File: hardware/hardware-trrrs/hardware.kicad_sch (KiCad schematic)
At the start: 81 parts, among them J2 Barrel_Jack, M1 Stepper_Motor_unipolar_5pin, M10 Stepper_Motor_unipolar_5pin, M11 Stepper_Motor_unipolar_5pin, M12 Stepper_Motor_unipolar_5pin, M13 Stepper_Motor_unipolar_5pin, M14 Stepper_Motor_unipolar_5pin, M2 Stepper_Motor_unipolar_5pin, M3 Stepper_Motor_unipolar_5pin, M4 Stepper_Motor_unipolar_5pin, M5 Stepper_Motor_unipolar_5pin, M6 Stepper_Motor_unipolar_5pin, M7 Stepper_Motor_unipolar_5pin, M8 Stepper_Motor_unipolar_5pin, M9 Stepper_Motor_unipolar_5pin, SW1 SW_Push_SPDT, SW10 SW_Push_SPDT, SW11 SW_Push_SPDT, SW12 SW_Push_SPDT, SW13 SW_Push_SPDT, SW14 SW_Push_SPDT, SW15 SW_Push_SPDT, SW16 SW_Push_SPDT, SW2 SW_Push_SPDT, SW3 SW_Push_SPDT, SW4 SW_Push_SPDT, SW5 SW_Push_SPDT, SW6 SW_Push_SPDT, SW7 SW_Push_SPDT, SW8 SW_Push_SPDT, SW9 SW_Push_SPDT, U1 WeMos_D1_mini, U10 ULN2003A, U11 ULN2003A, U12 ULN2003A, U13 ULN2003A, U14 ULN2003A, U15 ULN2003A, U16 ULN2003A, U17 ULN2003A, U2 CD4051B, U3 CD4051B, U4 ULN2003A, U5 ULN2003A, U6 ULN2003A, U7 ULN2003A, U8 ULN2003A, U9 ULN2003A

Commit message: added new pcb revision (trrrs)
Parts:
- added C15, C16: 10pF, Capacitor_SMD:C_0402_1005Metric, symbol Device:C
- added M15, M16: Stepper_Motor_unipolar_5pin, Connector_Audio:AUDIO-SMD_STX-3542-5N-G-TR, symbol Motor:Stepper_Motor_unipolar_5pin
- added U18, U19: ULN2003A, Package_SO:SOIC-16_3.9x9.9mm_P1.27mm, symbol Transistor_Array:ULN2003A
- C1, C10, C11, C12, C13, C14, C2, C3, C4, C5, C6, C7, C8, C9: footprint Capacitor_SMD:C_0805_2012Metric -> Capacitor_SMD:C_0402_1005Metric; LCSC PN C157608 -> C1545
- M1, M10, M11, M12, M13, M14, M2, M3, M4, M7, M8, M9: footprint Connector_Audio:HOOYA-PJ-3505A_C19190915-Jack_3.5mm_PJ31060-I_Horizontal -> Connector_Audio:AUDIO-SMD_STX-3542-5N-G-TR; LCSC PN C19190915 -> (none); LSCS PN (none) -> C157991
- M5, M6: footprint Connector_Audio:HOOYA-PJ-3505A_C19190915-Jack_3.5mm_PJ31060-I_Horizontal -> Connector_Audio:AUDIO-SMD_STX-3542-5N-G-TR; LSCS PN C19190915 -> C157991
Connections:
- net +5V: now also C15.1, C16.1, M15.1, M16.1, U18.9 (COM), U19.9 (COM)
- net GND: now also C15.2, C16.2, U18.8 (GND), U19.8 (GND)
- net IN1: now also U18.1 (I1), U19.1 (I1)
- net IN2: now also U18.2 (I2), U19.2 (I2)
- net IN3: now also U18.3 (I3), U19.3 (I3)
- net IN4: now also U18.4 (I4), U19.4 (I4)
- net PINK1: now also M1.4; no longer M1.3 (-)
- net PINK10: now also M10.4; no longer M10.3 (-)
- net PINK11: now also M11.4; no longer M11.3 (-)
- net PINK12: now also M12.4; no longer M12.3 (-)
- net PINK13: now also M13.4; no longer M13.3 (-)
- net PINK14: now also M14.4; no longer M14.3 (-)
- net PINK2: now also M2.4; no longer M2.3 (-)
- net PINK3: now also M3.4; no longer M3.3 (-)
- net PINK4: now also M4.4; no longer M4.3 (-)
- net PINK5: now also M5.4; no longer M5.3 (-)
- net PINK6: now also M6.4; no longer M6.3 (-)
- net PINK7: now also M7.4; no longer M7.3 (-)
- net PINK8: now also M8.4; no longer M8.3 (-)
- net PINK9: now also M9.4; no longer M9.3 (-)
- net YELLOW1: now also M1.3 (-); no longer M1.4
- net YELLOW10: now also M10.3 (-); no longer M10.4
- net YELLOW11: now also M11.3 (-); no longer M11.4
- net YELLOW12: now also M12.3 (-); no longer M12.4
- net YELLOW13: now also M13.3 (-); no longer M13.4
- net YELLOW14: now also M14.3 (-); no longer M14.4
- net YELLOW2: now also M2.3 (-); no longer M2.4
- net YELLOW3: now also M3.3 (-); no longer M3.4
- net YELLOW4: now also M4.3 (-); no longer M4.4
- net YELLOW5: now also M5.3 (-); no longer M5.4
- net YELLOW6: now also M6.3 (-); no longer M6.4
- net YELLOW7: now also M7.3 (-); no longer M7.4
- net YELLOW8: now also M8.3 (-); no longer M8.4
- net YELLOW9: now also M9.3 (-); no longer M9.4
- new net BLUE15: M15.5, U18.16 (O1)
- new net BLUE16: M16.5, U19.16 (O1)
- new net ORANGE15: M15.2, U18.13 (O4)
- new net ORANGE16: M16.2, U19.13 (O4)
- new net PINK15: M15.4, U18.15 (O2)
- new net PINK16: M16.4, U19.15 (O2)
- new net YELLOW15: M15.3 (-), U18.14 (O3)
- new net YELLOW16: M16.3 (-), U19.14 (O3)
- no-connect marks 89 -> 101
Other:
- note added: "CHOOSE YOUR COMPONENTS FROM HERE: https://jlcpcb.com/parts/2nd/Capacitors/Multilayer_Ceramic_Capacitors_MLCC_SMD_SMT_33?spm=search&searchTxt=10pf%20 the jlcpcb parts lib and not lcsc!!"
- note added: "good"
- moved on the sheet: C10, C11, C12, C13, C14, C5, C6, C7, C8, C9, U10, U11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

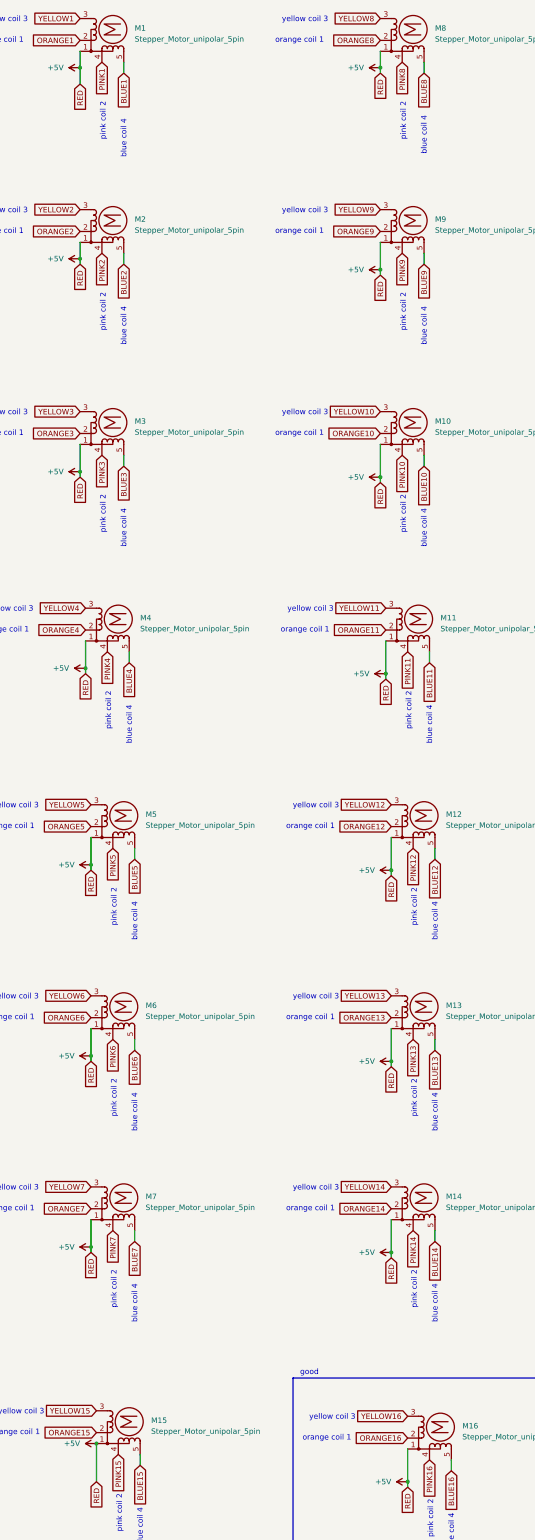
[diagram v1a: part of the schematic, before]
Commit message: Added do not populate flag to trrrs jacks
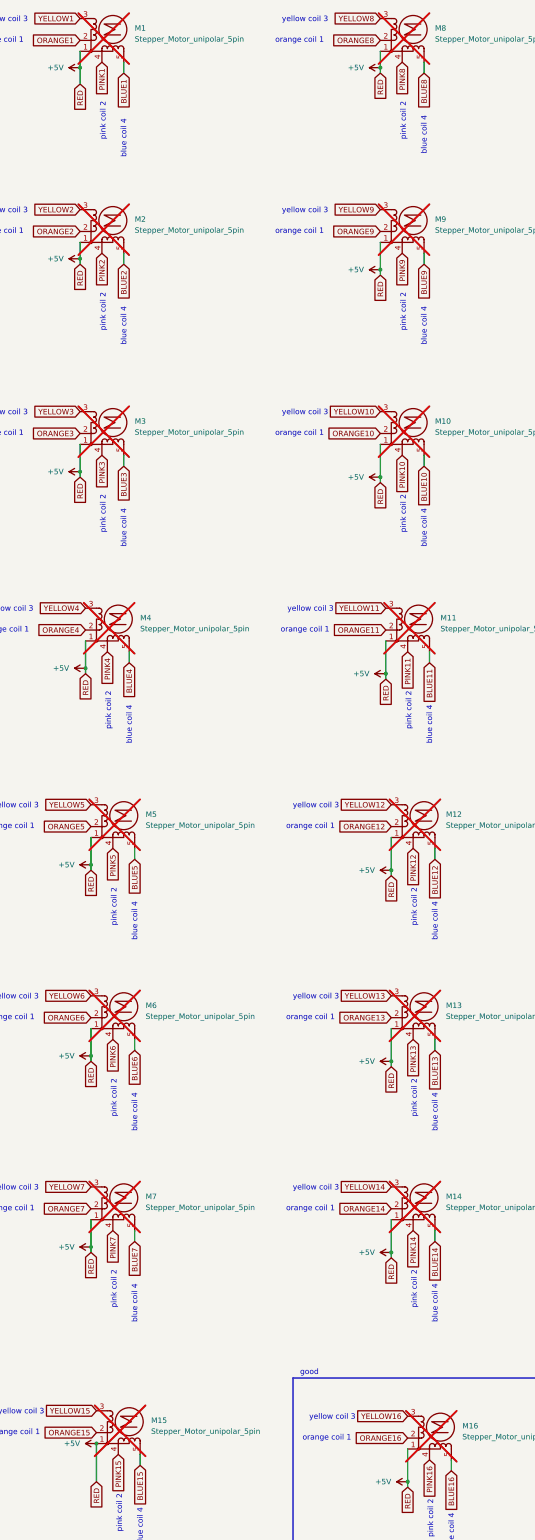
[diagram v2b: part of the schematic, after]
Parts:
- M1, M10, M11, M12, M13, M14, M15, M16, M2, M3, M4, M5, M6, M7, M8, M9: now not fitted
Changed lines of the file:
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@@
 		(in_bom yes)
 		(on_board yes)
-		(dnp no)
+		(dnp yes)
 		(fields_autoplaced yes)
 		(property "Reference" "M5"
@@
 		(in_bom yes)
 		(on_board yes)
-		(dnp no)
+		(dnp yes)
 		(fields_autoplaced yes)
 		(property "Reference" "M13"
@@
 		(in_bom yes)
 		(on_board yes)
-		(dnp no)
+		(dnp yes)
 		(fields_autoplaced yes)
 		(property "Reference" "M10"
@@
 		(in_bom yes)
 		(on_board yes)
-		(dnp no)
+		(dnp yes)
 		(fields_autoplaced yes)
 		(property "Reference" "M9"
@@
 		(in_bom yes)
 		(on_board yes)
-		(dnp no)
+		(dnp yes)
 		(fields_autoplaced yes)
 		(property "Reference" "M7"
@@
 		(in_bom yes)
 		(on_board yes)
-		(dnp no)
+		(dnp yes)
 		(fields_autoplaced yes)
 		(property "Reference" "M1"
@@
 		(in_bom yes)
 		(on_board yes)
-		(dnp no)
+		(dnp yes)
 		(fields_autoplaced yes)
 		(property "Reference" "M3"
@@
 		(in_bom yes)
 		(on_board yes)
-		(dnp no)
+		(dnp yes)
 		(fields_autoplaced yes)
 		(property "Reference" "M14"
@@
 		(in_bom yes)
 		(on_board yes)
-		(dnp no)
+		(dnp yes)
 		(fields_autoplaced yes)
 		(property "Reference" "M4"
@@
 		(in_bom yes)
 		(on_board yes)
-		(dnp no)
+		(dnp yes)
 		(fields_autoplaced yes)
 		(property "Reference" "M12"
@@
 		(in_bom yes)
 		(on_board yes)
-		(dnp no)
+		(dnp yes)
 		(fields_autoplaced yes)
 		(property "Reference" "M11"
@@
 		(in_bom yes)
 		(on_board yes)
-		(dnp no)
+		(dnp yes)
 		(fields_autoplaced yes)
 		(property "Reference" "M8"
@@
 		(in_bom yes)
 		(on_board yes)
-		(dnp no)
+		(dnp yes)
 		(fields_autoplaced yes)
 		(property "Reference" "M16"
@@
 		(in_bom yes)
 		(on_board yes)
-		(dnp no)
+		(dnp yes)
 		(fields_autoplaced yes)
 		(property "Reference" "M6"
@@
 		(in_bom yes)
 		(on_board yes)
-		(dnp no)
+		(dnp yes)
 		(fields_autoplaced yes)
 		(property "Reference" "M15"
@@
 		(in_bom yes)
 		(on_board yes)
-		(dnp no)
+		(dnp yes)
 		(fields_autoplaced yes)
 		(property "Reference" "M2"

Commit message: Added production files (Pick and Place) for JLCPCB
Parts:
- J2: now not fitted; now left out of the parts list
- M1, M10, M11, M12, M13, M14, M15, M16, M2, M3, M4, M5, M6, M7, M8, M9, SW6, SW7, SW8, SW9: now left out of the parts list
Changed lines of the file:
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@@
 		(unit 1)
 		(exclude_from_sim no)
-		(in_bom yes)
+		(in_bom no)
 		(on_board yes)
 		(dnp yes)
@@
 		(unit 1)
 		(exclude_from_sim no)
-		(in_bom yes)
+		(in_bom no)
 		(on_board yes)
 		(dnp yes)
@@
 		(unit 1)
 		(exclude_from_sim no)
-		(in_bom yes)
+		(in_bom no)
 		(on_board yes)
 		(dnp yes)
@@
 		(unit 1)
 		(exclude_from_sim no)
-		(in_bom yes)
+		(in_bom no)
 		(on_board yes)
 		(dnp yes)
@@
 		(unit 1)
 		(exclude_from_sim no)
-		(in_bom yes)
+		(in_bom no)
 		(on_board yes)
 		(dnp yes)
@@
 		(unit 1)
 		(exclude_from_sim no)
-		(in_bom yes)
+		(in_bom no)
 		(on_board yes)
 		(dnp yes)
@@
 		(unit 1)
 		(exclude_from_sim no)
-		(in_bom yes)
+		(in_bom no)
 		(on_board yes)
 		(dnp yes)
@@
 		(unit 1)
 		(exclude_from_sim no)
-		(in_bom yes)
+		(in_bom no)
 		(on_board yes)
 		(dnp yes)
@@
 		(unit 1)
 		(exclude_from_sim no)
-		(in_bom yes)
+		(in_bom no)
 		(on_board yes)
-		(dnp no)
+		(dnp yes)
 		(fields_autoplaced yes)
 		(property "Reference" "J2"
@@
 		(unit 1)
 		(exclude_from_sim no)
-		(in_bom yes)
+		(in_bom no)
 		(on_board yes)
 		(dnp yes)
@@
 		(unit 1)
 		(exclude_from_sim no)
-		(in_bom yes)
+		(in_bom no)
 		(on_board yes)
 		(dnp yes)
@@
 		(unit 1)
 		(exclude_from_sim no)
-		(in_bom yes)
+		(in_bom no)
 		(on_board yes)
 		(dnp yes)
@@
 		(unit 1)
 		(exclude_from_sim no)
-		(in_bom yes)
+		(in_bom no)
 		(on_board yes)
 		(dnp yes)
@@
 		(unit 1)
 		(exclude_from_sim no)
-		(in_bom yes)
+		(in_bom no)
 		(on_board yes)
 		(dnp yes)
@@
 		(unit 1)
 		(exclude_from_sim no)
-		(in_bom yes)
+		(in_bom no)
 		(on_board yes)
 		(dnp yes)
@@
 		(unit 1)
 		(exclude_from_sim no)
-		(in_bom yes)
+		(in_bom no)
 		(on_board yes)
 		(dnp yes)
@@
 		(unit 1)
 		(exclude_from_sim no)
-		(in_bom yes)
+		(in_bom no)
 		(on_board yes)
 		(dnp yes)
@@
 		(unit 1)
 		(exclude_from_sim no)
-		(in_bom yes)
+		(in_bom no)
 		(on_board yes)
 		(dnp yes)
@@
 		(unit 1)
 		(exclude_from_sim no)
-		(in_bom yes)
+		(in_bom no)
 		(on_board yes)
 		(dnp yes)
@@
 		(unit 1)
 		(exclude_from_sim no)
-		(in_bom yes)
+		(in_bom no)
 		(on_board yes)
 		(dnp yes)
@@
 		(unit 1)
 		(exclude_from_sim no)
-		(in_bom yes)
+		(in_bom no)
 		(on_board yes)
 		(dnp yes)
